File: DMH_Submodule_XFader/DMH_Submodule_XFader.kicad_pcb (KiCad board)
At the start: 2 copper layers, 45 x 45 mm, 47 parts, among them J1 Conn_01x04, J2 Conn_01x08, Q1 BC548, Q2 BC548, Q3 BC548, Q4 BC548, U1 TL074, U2 TL072

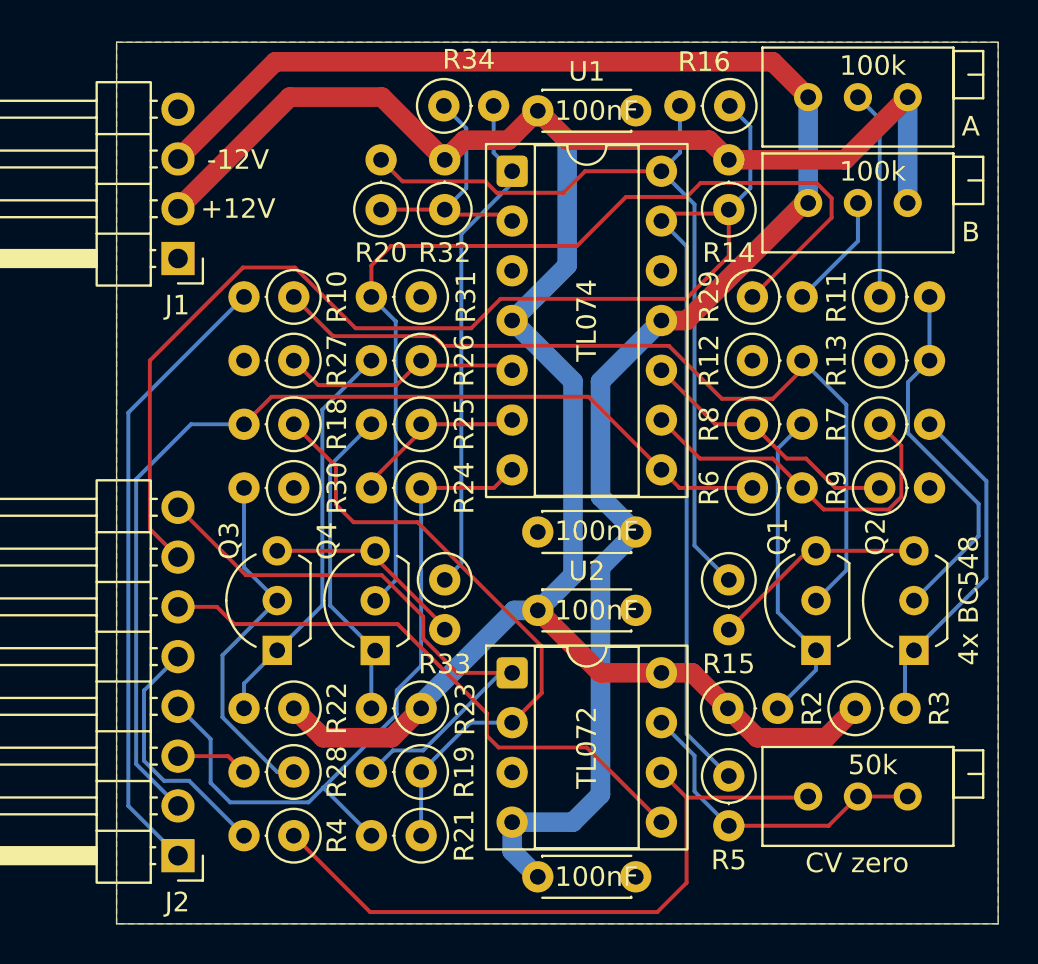
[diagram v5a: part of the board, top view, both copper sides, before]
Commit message: Added solder jumpers to X faders
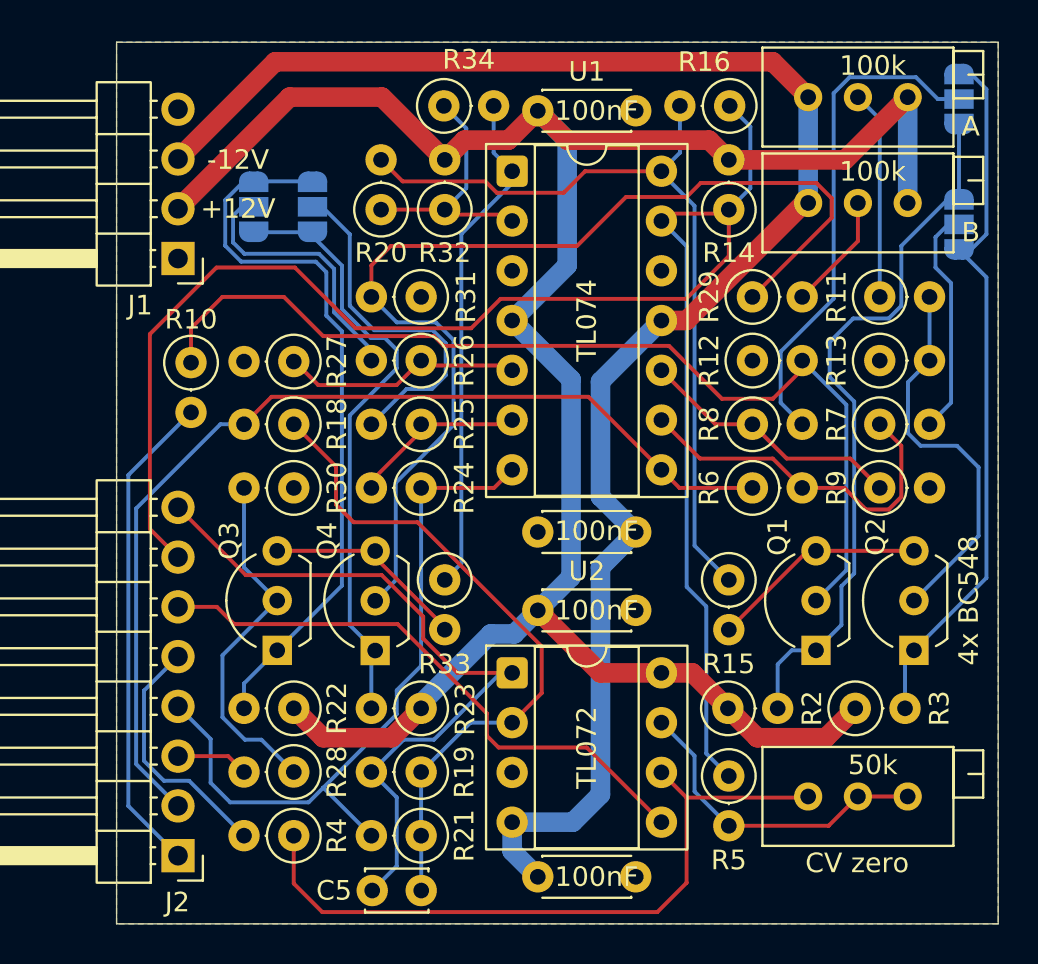
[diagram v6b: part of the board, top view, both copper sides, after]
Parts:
- added C5: 33pF, Capacitor_THT:C_Disc_D3.0mm_W2.0mm_P2.50mm, F.Cu at (70.0, 95.8)
- added JP1: SolderJumper_3_Open, Jumper:SolderJumper-3_P1.3mm_Open_RoundedPad1.0x1.5mm_NumberLabels, B.Cu at (97.5, 61.8)
- added JP2: SolderJumper_3_Open, Jumper:SolderJumper-3_P1.3mm_Open_RoundedPad1.0x1.5mm_NumberLabels, B.Cu at (97.5, 55.4)
- added JP3: SolderJumper_3_Open, Jumper:SolderJumper-3_P1.3mm_Open_RoundedPad1.0x1.5mm_NumberLabels, B.Cu at (64.5, 60.9)
- added JP4: SolderJumper_3_Open, Jumper:SolderJumper-3_P1.3mm_Open_RoundedPad1.0x1.5mm_NumberLabels, B.Cu at (61.5, 60.9)
- moved R10 6.23 mm to (58.3, 68.9), turned to -90 degrees
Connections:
- Q1 pad 1: Net-(Q1-C) -> Net-(JP1-B)
- Q2 pad 1: Net-(Q2-C) -> Net-(JP1-A)
- Q3 pad 1: Net-(Q3-C) -> Net-(JP3-B)
- Q4 pad 1: Net-(Q4-C) -> Net-(JP3-A)
- R2 pad 2: Net-(Q1-C) -> Net-(JP1-B)
- R22 pad 2: Net-(Q3-C) -> Net-(JP3-B)
- R23 pad 2: Net-(Q4-C) -> Net-(JP3-A)
- R25 pad 2: Net-(Q4-C) -> Net-(JP3-C)
- R26 pad 2: Net-(Q3-C) -> Net-(JP4-C)
- R3 pad 2: Net-(Q2-C) -> Net-(JP1-A)
- R7 pad 2: Net-(Q2-C) -> Net-(JP1-C)
- R8 pad 2: Net-(Q1-C) -> Net-(JP2-C)
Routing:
- net Net-(JP3-B): track 0.00 -> 37.6 mm
- net Net-(JP1-B): track 0.00 -> 36.8 mm
- net Net-(JP1-A): track 0.00 -> 36.6 mm
- net Net-(JP3-A): track 0.00 -> 31.1 mm
- net Net-(JP2-C): track 0.00 -> 25.7 mm
- net Net-(Q3-C): track 20.4 -> 0.00 mm
- net Net-(JP3-C): track 0.00 -> 18.3 mm
- net Net-(Q2-C): track 17.4 -> 0.00 mm
- net Net-(Q1-C): track 16.6 -> 0.00 mm
- net Net-(Q4-C): track 16.4 -> 0.00 mm
- net Net-(JP4-C): track 0.00 -> 13.8 mm
- net Net-(JP1-C): track 0.00 -> 11.8 mm
- net Net-(Q1-B): track 43.0 -> 50.7 mm
- net /Out_X: track 30.5 -> 37.6 mm
- net /In_A: track 32.0 -> 25.0 mm
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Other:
- board text added: "Mk1.0 - October 2026"
- board text removed: "Mk1.0 - July 2026"
